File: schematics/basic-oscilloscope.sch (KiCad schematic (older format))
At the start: 1 part

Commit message: add voltage buffer for BNC channels
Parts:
- removed U?: 74AHC1G4210, Package_TO_SOT_SMD:SOT-353_SC-70-5, symbol 74xGxx:74AHC1G4210
- added C1, C11, C12, C6: 100n, symbol Device:CP
- added C10, C7, C8, C9, C?: 100p, symbol Device:CP
- added C2, C4: CP, symbol Device:CP
- added C3, C5: 10u, symbol Device:CP
- added C? (x5): 0.1u, symbol Device:CP
- added D1: LED, symbol Device:LED
- added D2, D3: 1N4001, Diode_THT:D_DO-41_SOD81_P10.16mm_Horizontal, symbol Diode:1N4001
- added J1: 9V_BATTERY, symbol Connector:Screw_Terminal_01x02
- added J2: 12V_DC_JACK, symbol Connector:Barrel_Jack
- added J?: CH1, symbol Connector:Conn_Coaxial
- added J?: CH2, symbol Connector:Conn_Coaxial
- added R1: 200, symbol Device:R
- added R2, R3, R?: 100k, symbol Device:R
- added R4: 10k, symbol Device:R
- added R5, R6: 22R, symbol Device:R
- added R? (x5): 1k, symbol Device:R
- added SW? (x6): SW_Push, symbol Switch:SW_Push
- added SW?: SW_SPST, symbol Switch:SW_SPST
- added U1: LT3032-3.3, Package_DFN_QFN:Linear_DE14MA, symbol Regulator_Linear:LT3032-3.3
- added U2: STM32F103C8Tx, Package_QFP:LQFP-48_7x7mm_P0.5mm, symbol MCU_ST_STM32F1:STM32F103C8Tx
- added U?: TL082, symbol Amplifier_Operational:TL082
- added U? (x5): 74HC14, symbol 74xx:74HC14
- added Y1, Y2: Crystal, symbol Device:Crystal
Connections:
- net labels added: +, +3.3V, -, 0, 3.3V, ACT_BUF, BOOT_0, BOOT_1, GND, HOLD_RUN, RESET, SEL_OK, TO_BUF, TO_BUF2, USBDM, USBDP
- wire segments 0 -> 92
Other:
- note added: "CONNECTORS\n"
- note added: "CONTROL\n"
- note added: "DO: Activate pull-ups for GPIO in code"
- note added: "LEDs"
- note added: "MPU"
- note added: "POWER SUPPLY"
- note added: "RESET"

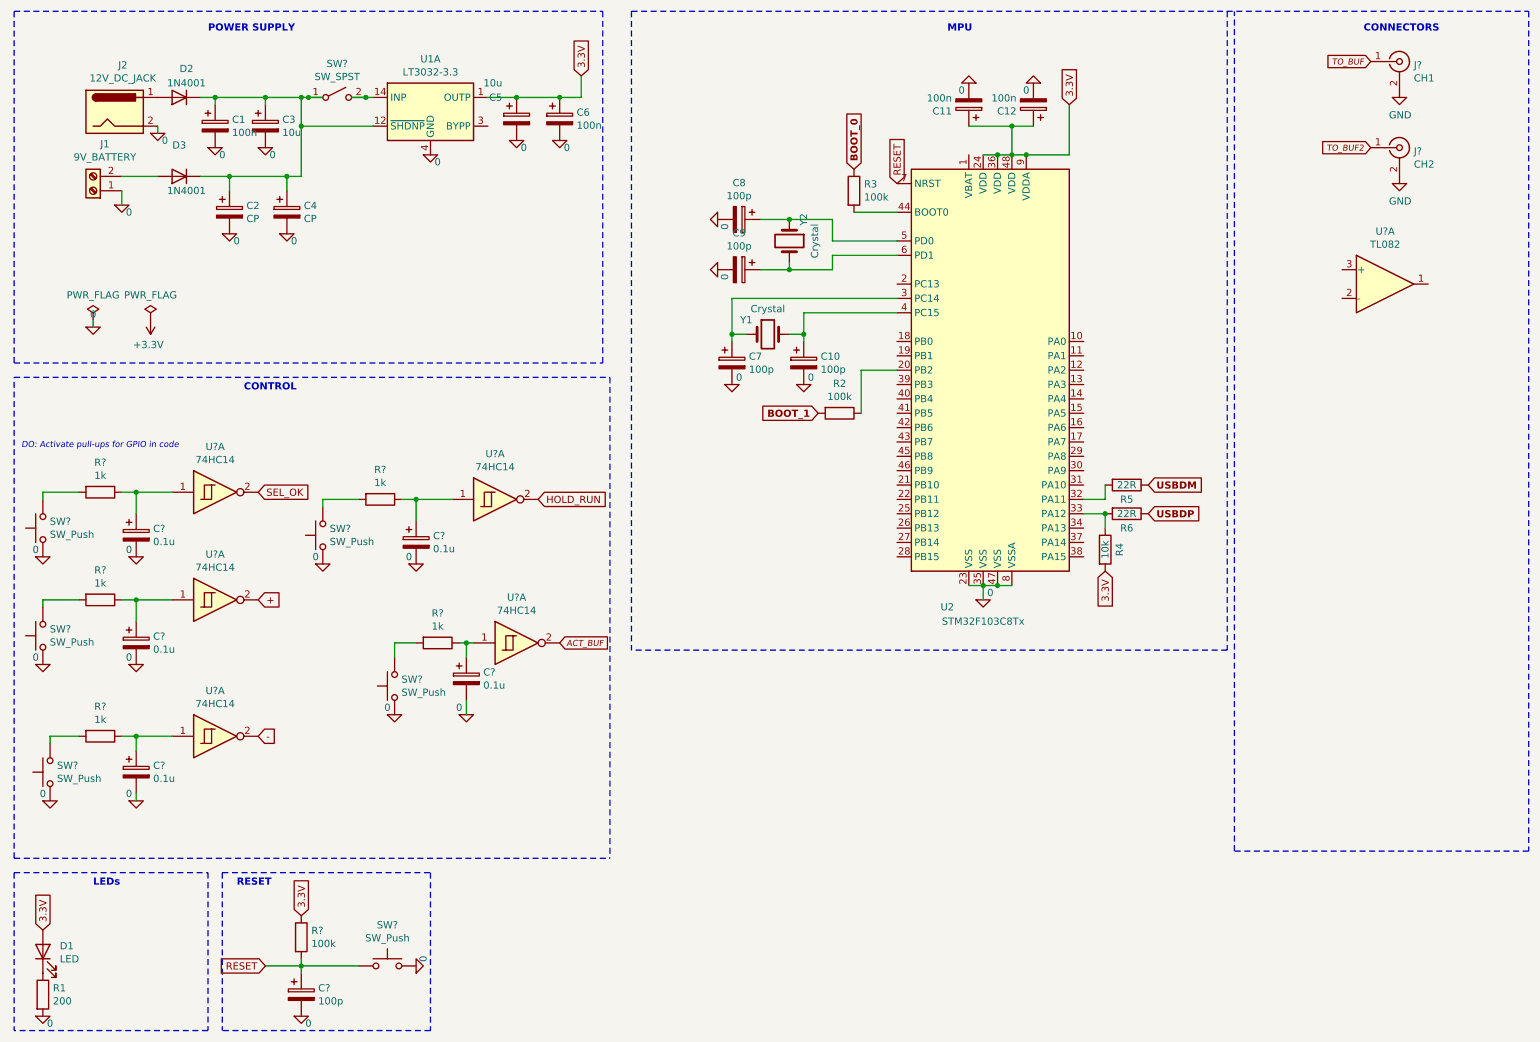
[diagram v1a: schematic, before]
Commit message: add 5V label for buffer
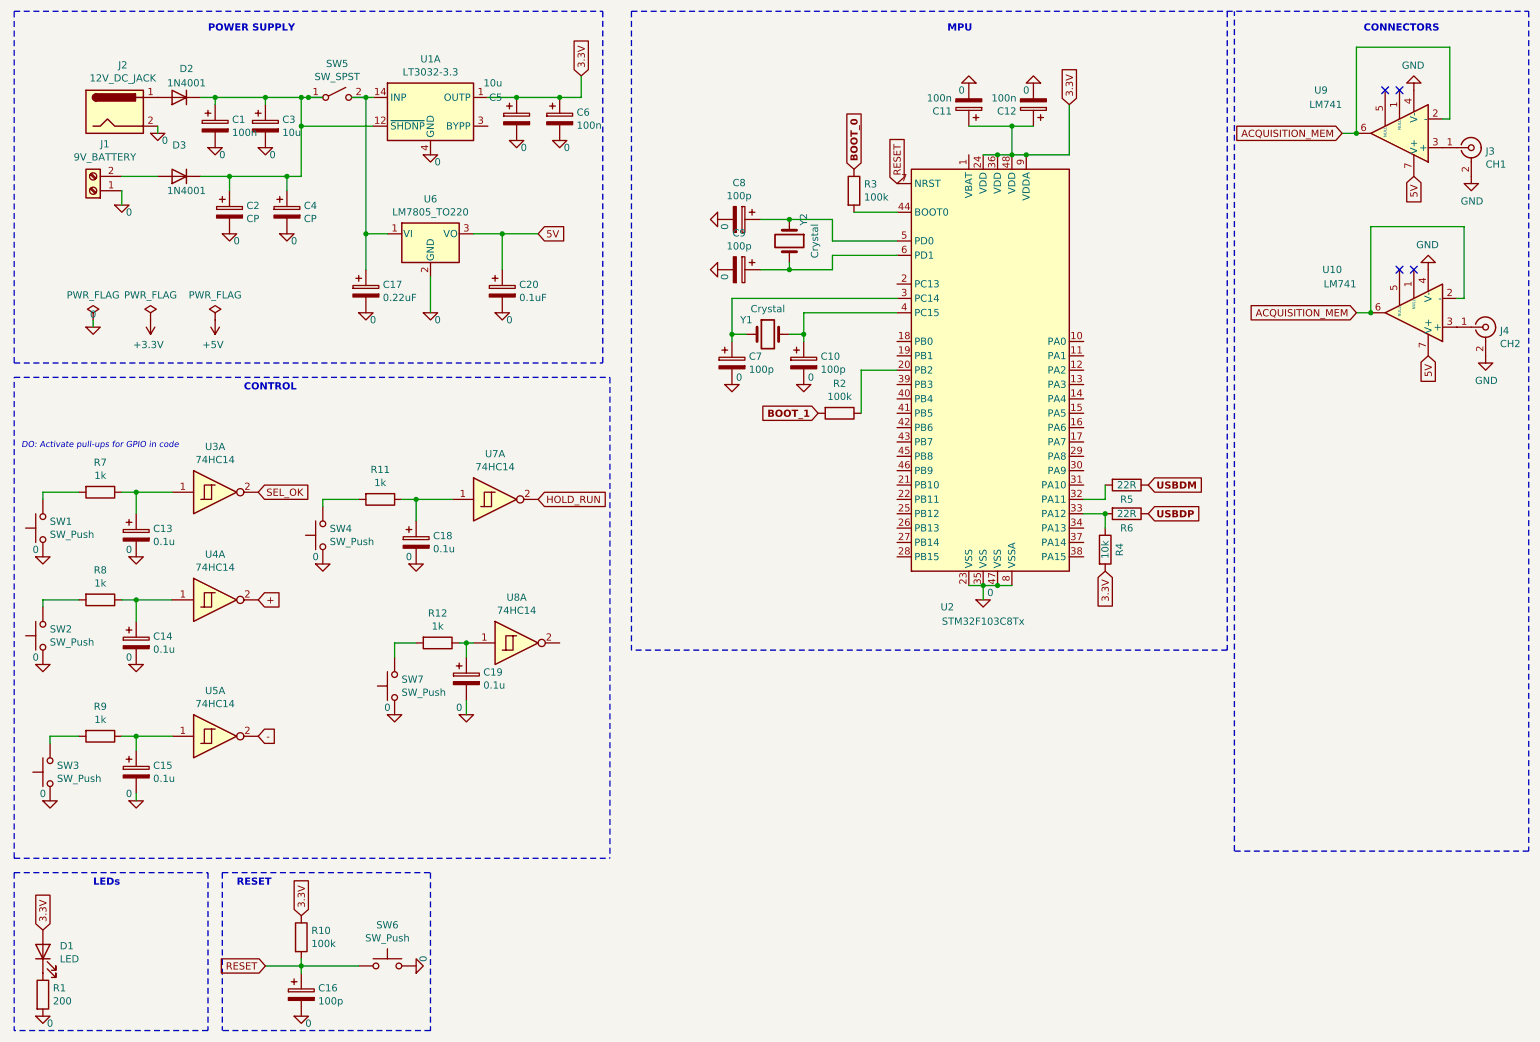
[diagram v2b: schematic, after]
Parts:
- removed U?: TL082, symbol Amplifier_Operational:TL082
- added C17: 0.22uF, symbol Device:CP
- added C20: 0.1uF, symbol Device:CP
- added U10, U9: LM741, symbol Amplifier_Operational:LM741
- added U6: LM7805_TO220, Package_TO_SOT_THT:TO-220-3_Vertical, symbol Regulator_Linear:LM7805_TO220
- gave numbers to parts that had none: 26
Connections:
- net 0: now also C17.2, C20.2, U6.2 (GND)
- net GND: now also U10.4 (V-), U9.4 (V-)
- net at SW5.2 (B), U1.14 (INP): now also C17.1, U6.1 (VI)
- net ACT_BUF: no longer names the net of U8.2
- net TO_BUF: no longer names the net of J3.1 (In)
- net TO_BUF: now also U9.3 (+)
- net TO_BUF2: no longer names the net of J4.1 (In)
- net TO_BUF2: now also U10.3 (+)
- new net 5V: C20.1, U10.7 (V+), U6.3 (VO), U9.7 (V+)
- new net ACQUISITION_MEM: U10.2 (-), U10.6, U9.2 (-), U9.6
- no-connect marks 0 -> 4
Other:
- moved on the sheet: J3, J4

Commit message: create pcb layout
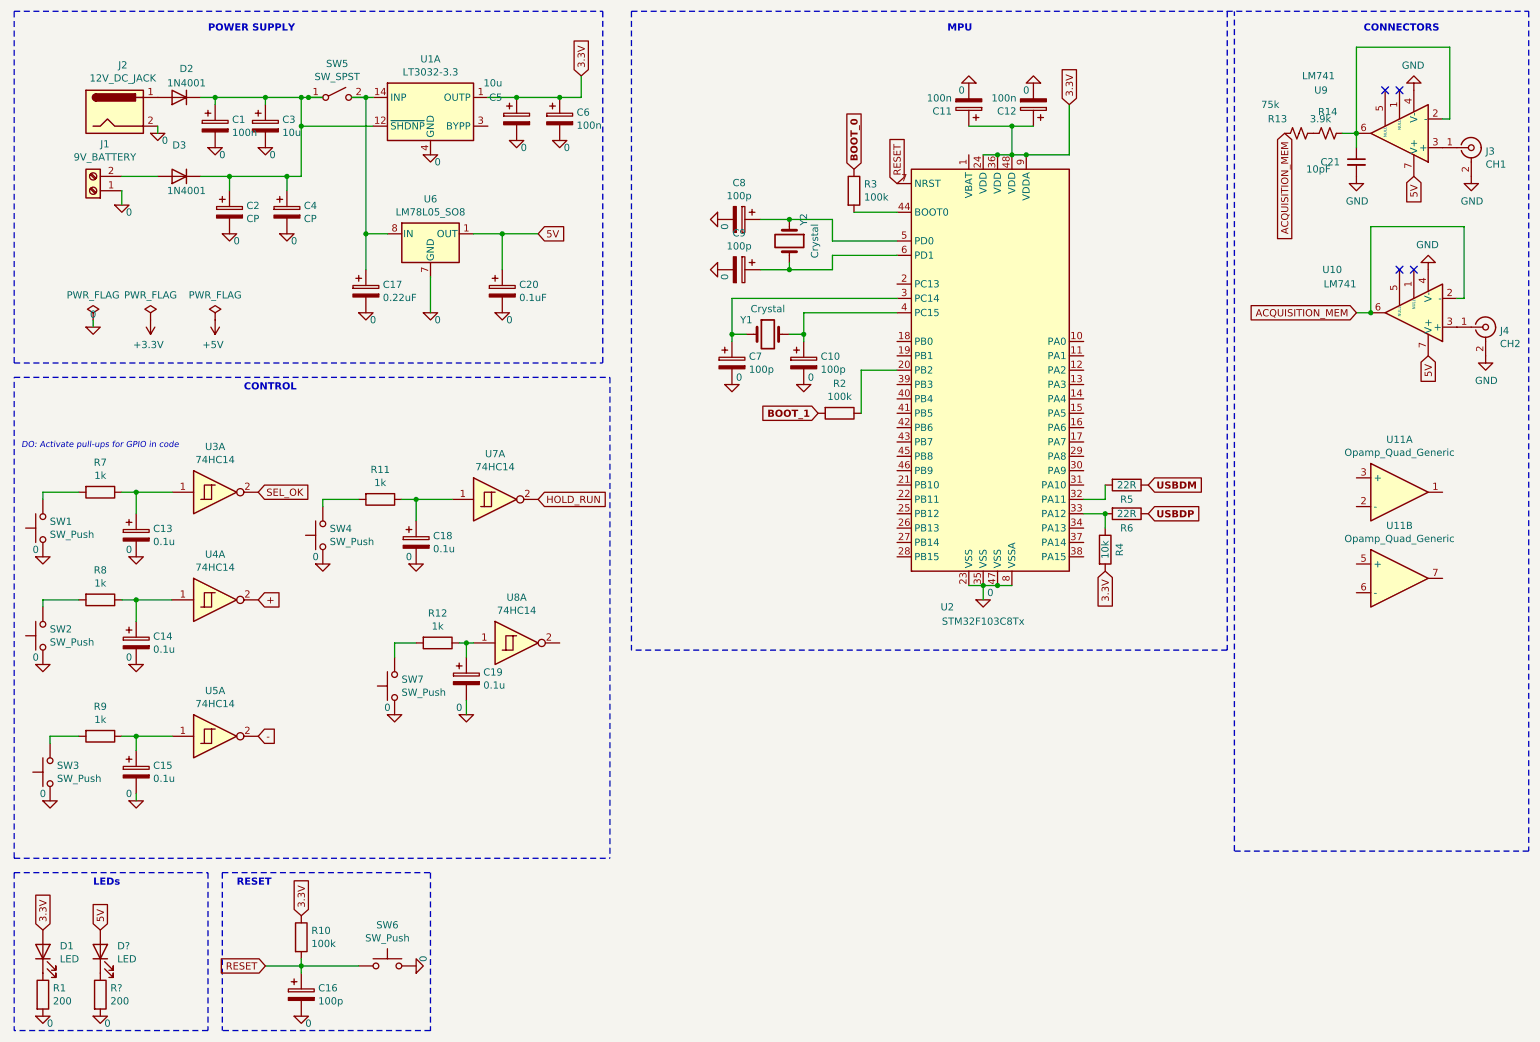
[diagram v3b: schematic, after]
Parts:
- removed U6: LM7805_TO220, Package_TO_SOT_THT:TO-220-3_Vertical, symbol Regulator_Linear:LM7805_TO220
- added C21: 10pF, symbol Device:C_Small
- added D?: LED, Diode_SMD:D_0603_1608Metric, symbol Device:LED
- added R13: 75k, symbol Device:R_Small_US
- added R14: 3.9k, symbol Device:R_Small_US
- added R?: 200, Resistor_SMD:R_0603_1608Metric, symbol Device:R
- added U11: Opamp_Quad_Generic, symbol Device:Opamp_Quad_Generic
- added U6: LM78L05_SO8, Package_SO:SOIC-8_3.9x4.9mm_P1.27mm, symbol Regulator_Linear:LM78L05_SO8
- C1, C2, C3, C4, C5, C6: footprint (none) -> Capacitor_SMD:C_0603_1608Metric
- D1: footprint (none) -> Diode_SMD:D_0603_1608Metric
- D2, D3: footprint Diode_THT:D_DO-41_SOD81_P10.16mm_Horizontal -> Diode_SMD:D_0603_1608Metric
- J1: footprint (none) -> TerminalBlock:TerminalBlock_Altech_AK300-2_P5.00mm
- J2: footprint (none) -> Connector_BarrelJack:BarrelJack_Wuerth_6941xx301002
- R1: footprint (none) -> Resistor_SMD:R_0603_1608Metric
- SW5: footprint (none) -> Button_Switch_THT:SW_DIP_SPSTx01_Slide_9.78x4.72mm_W7.62mm_P2.54mm
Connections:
- net 0: now also R?.2, U6.2 (GND), U6.3 (GND), U6.6 (GND), U6.7 (GND)
- net 5V: now also D?.2 (A), U6.1 (OUT)
- net ACQUISITION_MEM: now also R13.2; no longer U9.2 (-), U9.6
- net GND: now also C21.2
- net at C17.1, SW5.2 (B), U1.14 (INP): now also U6.8 (IN)
- new net: C21.1, R14.1, U9.2 (-), U9.6
- new net: R13.1, R14.2
- new net: D?.1 (K), R?.1

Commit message: update component footprints
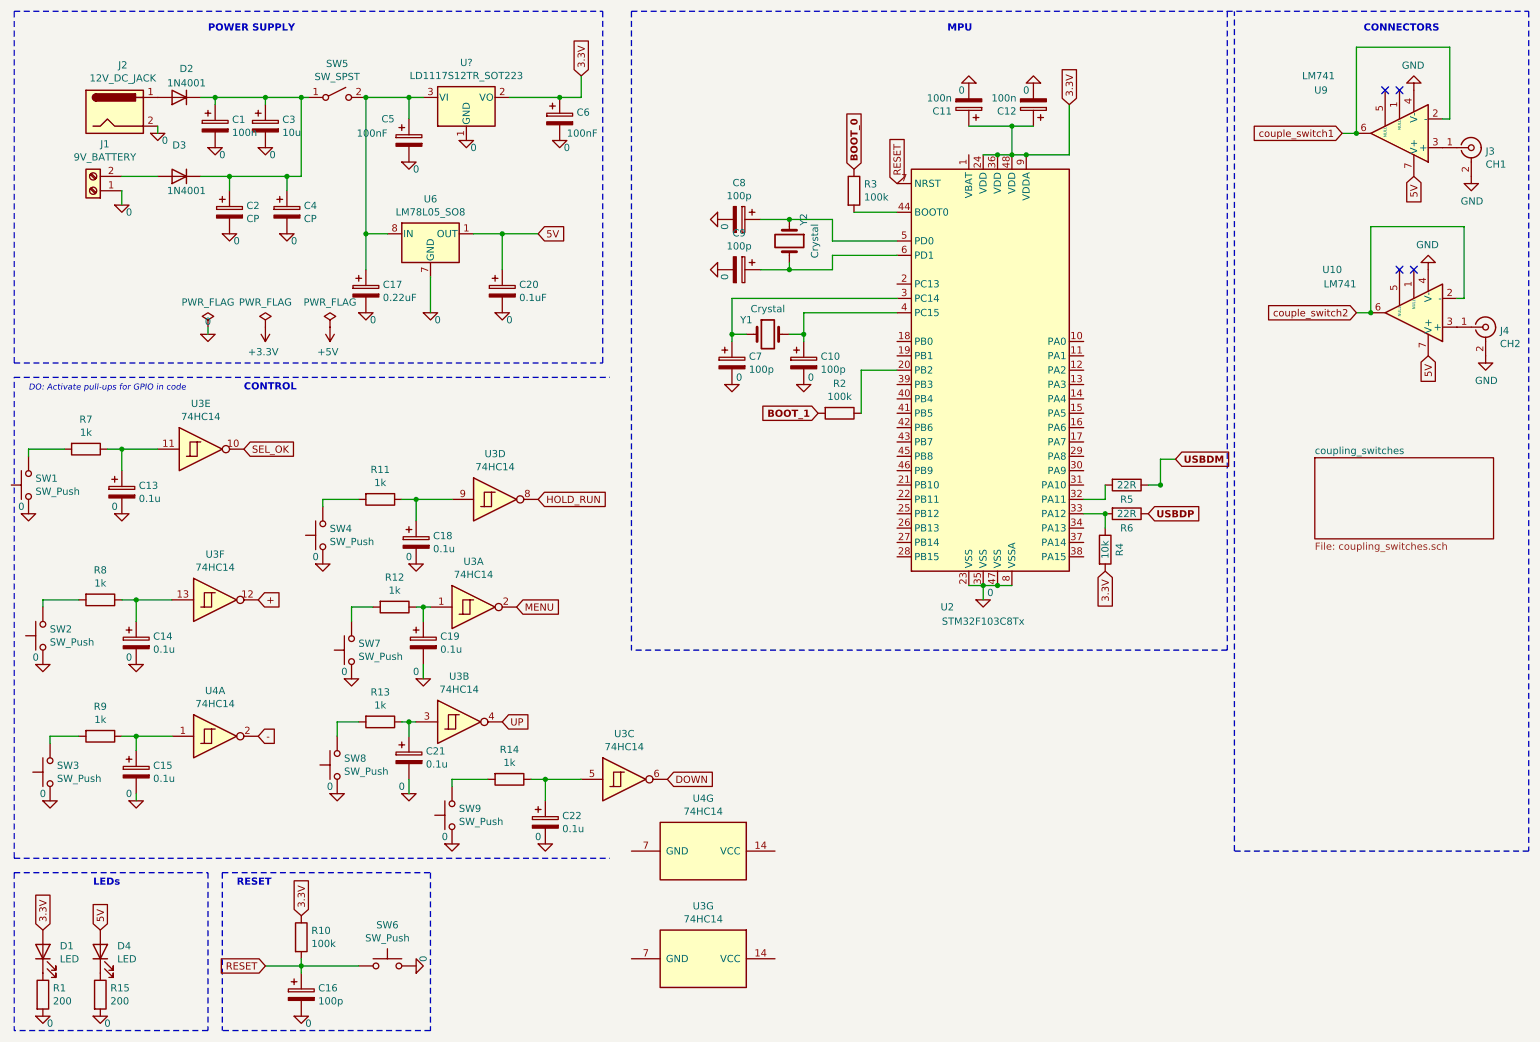
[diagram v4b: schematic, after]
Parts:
- removed C21: 10pF, symbol Device:C_Small
- removed R13: 75k, symbol Device:R_Small_US
- removed R14: 3.9k, symbol Device:R_Small_US
- removed U1: LT3032-3.3, Package_DFN_QFN:Linear_DE14MA, symbol Regulator_Linear:LT3032-3.3
- removed U11: Opamp_Quad_Generic, symbol Device:Opamp_Quad_Generic
- removed U5, U7, U8: 74HC14, symbol 74xx:74HC14
- added C21, C22: 0.1u, Capacitor_THT:CP_Radial_D4.0mm_P2.00mm, symbol Device:CP
- added R13, R14: 1k, symbol Device:R
- added SW8, SW9: SW_Push, symbol Switch:SW_Push
- added unit 2 of U3
- added unit 3 of U3
- added unit 4 of U3
- added unit 5 of U3
- added unit 6 of U3
- added unit 7 of U3
- added unit 7 of U4
- added U?: LD1117S12TR_SOT223, Package_TO_SOT_THT:TO-220-3_Vertical, symbol Regulator_Linear:LD1117S12TR_SOT223
- C1, C2, C3, C4: footprint Capacitor_SMD:C_0603_1608Metric -> Capacitor_THT:CP_Radial_D4.0mm_P2.00mm
- C10, C11, C12, C13, C14, C16, C17, C18, C19, C20, C7, C8, C9: footprint (none) -> Capacitor_THT:CP_Radial_D4.0mm_P2.00mm
- C5: value 10u -> 100nF; footprint Capacitor_SMD:C_0603_1608Metric -> Capacitor_THT:CP_Radial_D4.0mm_P2.00mm
- C6: value 100n -> 100nF; footprint Capacitor_SMD:C_0603_1608Metric -> Capacitor_THT:CP_Radial_D4.0mm_P2.00mm
- D2: footprint Diode_SMD:D_0603_1608Metric -> Diode_THT:D_DO-34_SOD68_P7.62mm_Horizontal
- U6: footprint Package_SO:SOIC-8_3.9x4.9mm_P1.27mm -> Package_TO_SOT_THT:TO-220-3_Vertical
- gave numbers to parts that had none: 2
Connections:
- net +: now also U3.12; no longer U4.2
- net -: now also U4.2
- net 0: now also C21.2, C22.2, SW8.1, SW9.1, U?.1 (GND)
- net 3.3V: now also U?.2 (VO); no longer C5.1
- net HOLD_RUN: now also U3.8
- net SEL_OK: now also U3.10; no longer U3.2
- net at C17.1, SW5.2 (B), U6.8 (IN): now also C5.1, U?.3 (VI)
- net couple_switch1: now reaches U9.2 (-), U9.6
- net at C13.1, R7.1: now also U3.11; no longer U3.1
- net at C14.1, R8.1: now also U3.13; no longer U4.1
- net at C18.1, R11.1: now also U3.9
- net at C15.1, R9.1: now also U4.1
- net at C19.1, R12.1: now also U3.1
- net ACQUISITION_MEM renamed couple_switch2
- new net: C21.1, R13.1, U3.3
- new net: R13.2, SW8.2
- new net: R14.2, SW9.2
- new net: C22.1, R14.1, U3.5
- new net DOWN: U3.6
- new net MENU: U3.2
- new net UP: U3.4
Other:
- moved on the sheet: C13, C19, C5, R12, R7, SW1, SW7
